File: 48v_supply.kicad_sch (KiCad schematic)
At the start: 39 parts, among them Q1 PXN020-100QSJ, Q2 TPH4R50ANH1,LQ, U1 LV5144RGYR

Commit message: Some mounting holes. Release to prod
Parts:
- U1: footprint VQFN20_RGY_TEX -> LV5144:VQFN20_RGY_TEX
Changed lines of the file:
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@@
 			)
 		)
-		(property "Footprint" "VQFN20_RGY_TEX"
+		(property "Footprint" "LV5144:VQFN20_RGY_TEX"
 			(at 80.01 74.93 0)
 			(effects

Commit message: Added DK order numbers
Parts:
- C1: DK (none) -> 399-14996-1-ND
- C10: DK (none) -> 1276-6807-1-ND
- C11: DK (none) -> 1276-1134-1-ND
- C12: DK (none) -> 1276-1006-1-ND
- C13, C14, C15, C16, C17: DK (none) -> 587-3718-1-ND
- C18: DK (none) -> 478-KGM15BR71E473KTCT-ND
- C19: DK (none) -> 478-KGM15ACG1H100JTCT-ND
- C2, C3, C4, C5, C8, C9: DK (none) -> 587-5039-1-ND
- C6: DK (none) -> 490-1355-1-ND
- C7: DK (none) -> 490-11477-1-ND
- D1, D2: DK (none) -> SML-D12M1WT86CT-ND
- L1: DK (none) -> P17073CT-ND
- Q1: DK (none) -> 1727-PXN020-100QSJCT-ND
- Q2: DK (none) -> 264-TPH4R50ANH1LQCT-ND
- R1: DK (none) -> 311-150HRCT-ND
- R10, R9: DK (none) -> 541-0.0GCT-ND
- R11, R12, R6: DK (none) -> 311-17.8KHRCT-ND
- R2, R7: DK (none) -> 311-23.2KHRCT-ND
- R3: DK (none) -> 311-4.42KHRCT-ND
- R4: DK (none) -> 311-7.50KHRCT-ND
- R5: DK (none) -> 311-100KHRCT-ND
- R8: DK (none) -> 311-499HRCT-ND
- TP1, TP2: DK (none) -> -
- U1: DK (none) -> 296-LV5144RGYRCT-ND

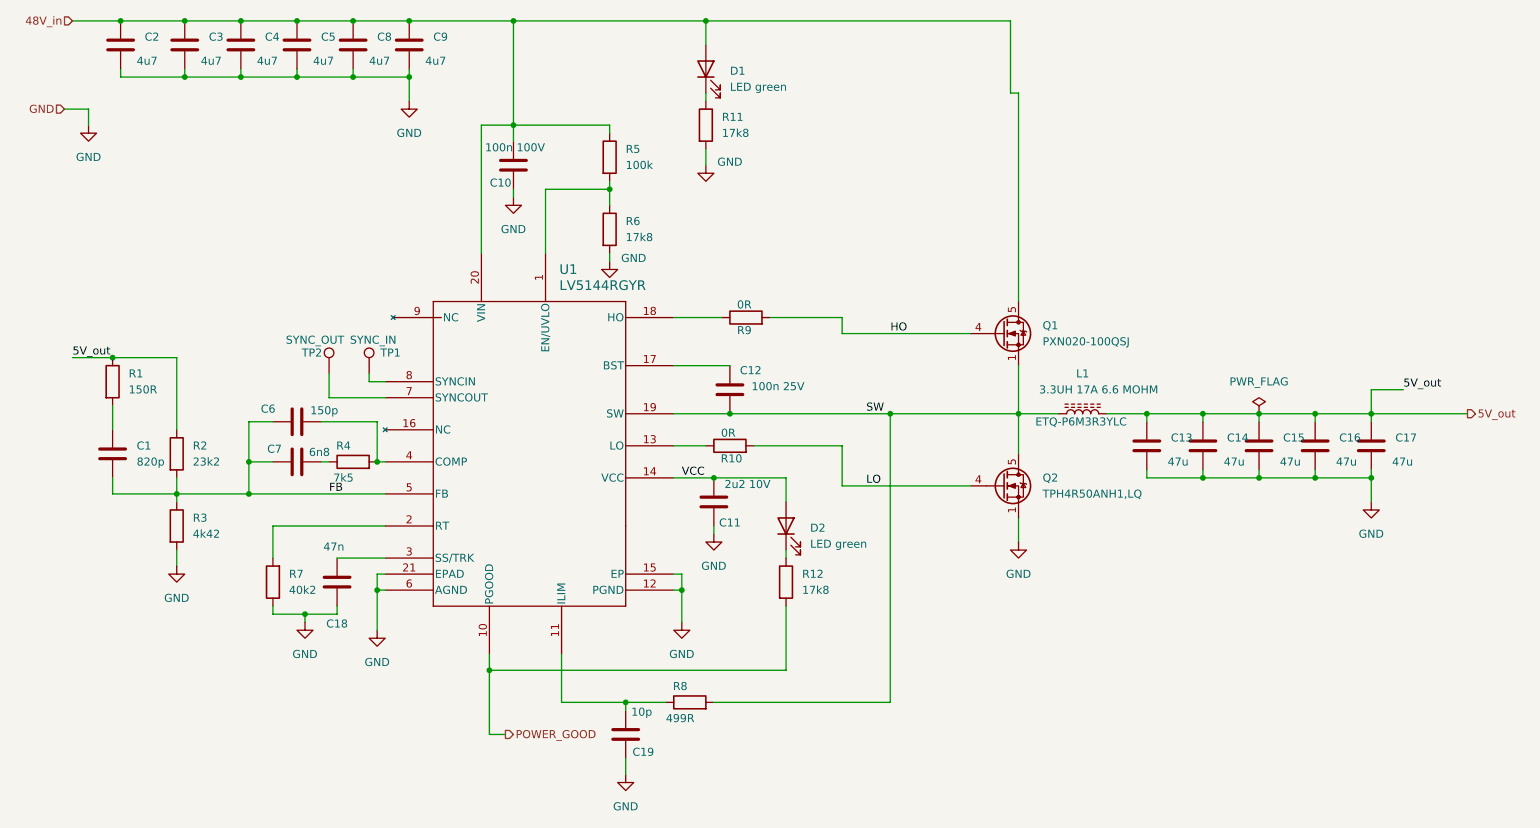
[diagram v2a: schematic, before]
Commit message: Minor updates and JLCPCB component codes added
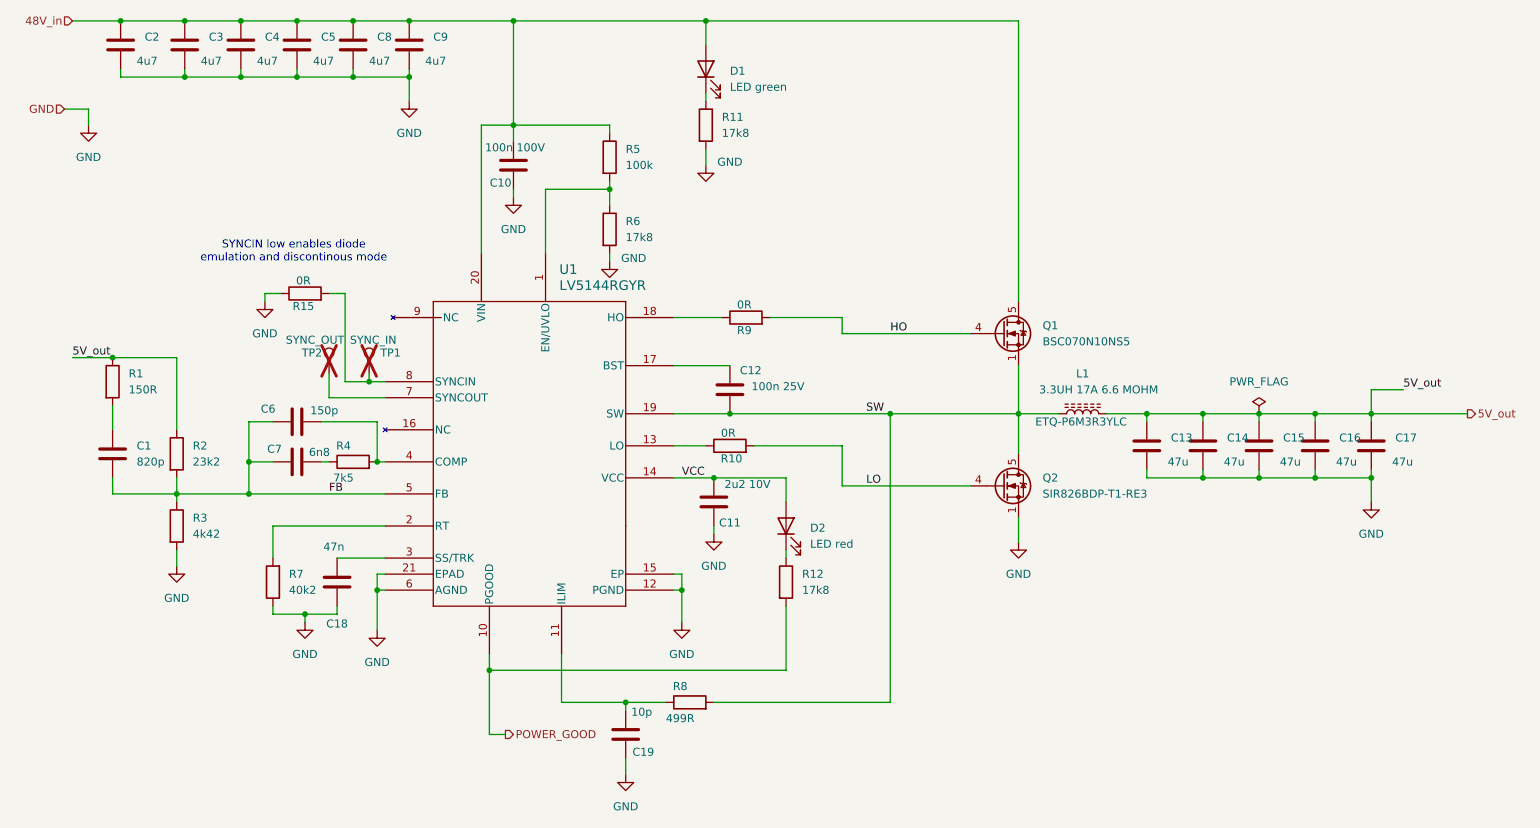
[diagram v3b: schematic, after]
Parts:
- added R15: 0R, Resistor_SMD:R_0603_1608Metric, symbol Device:R
- C1: LCSC (none) -> C14663
- C10: footprint Capacitor_SMD:C_0603_1608Metric -> Capacitor_SMD:C_0805_2012Metric; LCSC (none) -> C28233
- C11: LCSC (none) -> C23630
- C12: footprint Capacitor_SMD:C_0603_1608Metric -> Capacitor_SMD:C_0805_2012Metric; DK 1276-1006-1-ND -> 478-KGM21NR71E104KTCT-ND; LCSC (none) -> C28233
- C13, C14, C15, C16, C17: LCSC (none) -> C77101
- C18: LCSC (none) -> C107093
- C19: LCSC (none) -> C106245
- C2, C3, C4, C5, C8, C9: LCSC (none) -> C381466
- C6: LCSC (none) -> C107038
- C7: LCSC (none) -> C1631
- D1: footprint LED_SMD:LED_0603_1608Metric -> LED_SMD:LED_0805_2012Metric_Pad1.15x1.40mm_HandSolder; LCSC (none) -> C965815
- D2: value LED green -> LED red; footprint LED_SMD:LED_0603_1608Metric -> LED_SMD:LED_0805_2012Metric_Pad1.15x1.40mm_HandSolder; LCSC (none) -> C94741
- L1: LCSC (none) -> C542341
- Q1: value PXN020-100QSJ -> BSC070N10NS5; DK 1727-PXN020-100QSJCT-ND -> BSC070N10NS5ATMA1CT-ND; LCSC (none) -> C534364; MPN PXN020-100QSJ -> BSC070N10NS5
- Q2: value TPH4R50ANH1,LQ -> SIR826BDP-T1-RE3; LCSC (none) -> C6296763
- R1: LCSC (none) -> C22808
- R11, R12, R6: LCSC (none) -> C2933161
- R2: LCSC (none) -> C23346
- R3: LCSC (none) -> C2933223
- R4: LCSC (none) -> C114634
- R5: LCSC (none) -> C14675
- R7: LCSC (none) -> C2933218
- R8: LCSC (none) -> C23065
- TP1, TP2: now not fitted
- U1: JLCPCB (none) -> C34042097
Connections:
- net GND: now also R15.1
- net at TP1.1, U1.8 (SYNCIN): now also R15.2
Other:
- note added: "SYNCIN low enables diode emulation and discontinous mode"

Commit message: Added SPI ESP32-Pico. Last component JLCPCB codes
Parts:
- L1: LCSC C542341 -> C149539
- U1: LCSC (none) -> C34042097
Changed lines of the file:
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@@
+			)
+		)
+		(property "LCSC" "C34042097"
+			(at 80.01 74.93 0)
+			(effects
+				(font
+					(size 1.27 1.27)
+				)
+				(hide yes)
 			)
 		)
@@
 			)
 		)
-		(property "LCSC" "C542341"
+		(property "LCSC" "C149539"
 			(at 190.5 87.63 0)
 			(effects

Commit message: Added comment about 5V direct supply
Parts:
- L1: value 3.3UH 17A 6.6 MOHM -> 3.3UH 17A 6.6 MOHM
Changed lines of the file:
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@@
 (kicad_sch
-	(version 20231120)
+	(version 20250114)
 	(generator "eeschema")
-	(generator_version "8.0")
+	(generator_version "9.0")
 	(paper "A4")
+	(text "SYNCIN low enables diode\nemulation and discontinous mode\n"
+		(exclude_from_sim no)
+		(at 65.532 61.976 0)
+		(effects
+			(font
+				(size 1.27 1.27)
+			)
+		)
+	)
 	(junction
 		(at 236.22 97.79)
@@
 		)
 	)
-	(text "SYNCIN low enables diode\nemulation and discontinous mode\n"
-		(exclude_from_sim no)
-		(at 65.532 61.976 0)
-		(effects
-			(font
-				(size 1.27 1.27)
-			)
-		)
-	)
 	(label "LO"
 		(at 156.21 99.06 0)
-		(fields_autoplaced yes)
 		(effects
 			(font
@@
 	(label "5V_out"
 		(at 241.3 83.82 0)
-		(fields_autoplaced yes)
 		(effects
 			(font
@@
 	(label "VCC"
 		(at 127 97.79 0)
-		(fields_autoplaced yes)
 		(effects
 			(font
@@
 	(label "5V_out"
 		(at 30.48 78.74 0)
-		(fields_autoplaced yes)
 		(effects
 			(font
@@
 	(label "FB"
 		(at 71.12 100.33 0)
-		(fields_autoplaced yes)
 		(effects
 			(font
@@
 	(label "SW"
 		(at 156.21 87.63 0)
-		(fields_autoplaced yes)
 		(effects
 			(font
@@
 	(label "HO"
 		(at 160.02 74.93 0)
-		(fields_autoplaced yes)
 		(effects
 			(font
@@
 		(shape output)
 		(at 99.06 138.43 0)
-		(fields_autoplaced yes)
 		(effects
 			(font
@@
 		(shape input)
 		(at 30.48 25.4 180)
-		(fields_autoplaced yes)
 		(effects
 			(font
@@
 		(shape input)
 		(at 29.21 39.37 180)
-		(fields_autoplaced yes)
 		(effects
 			(font
@@
 		(shape output)
 		(at 251.46 87.63 0)
-		(fields_autoplaced yes)
 		(effects
 			(font
@@
 			)
 		)
-		(property "Value" "3.3UH 17A 6.6 MOHM "
+		(property "Value" "3.3UH 17A 6.6 MOHM"
 			(at 193.04 83.82 90)
 			(effects
